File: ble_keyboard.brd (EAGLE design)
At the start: 50.7 x 23.2 mm, 23 parts, among them Q1 DMG6968U-7, Q2 DMG2305UX-7, U1 YJ-14015

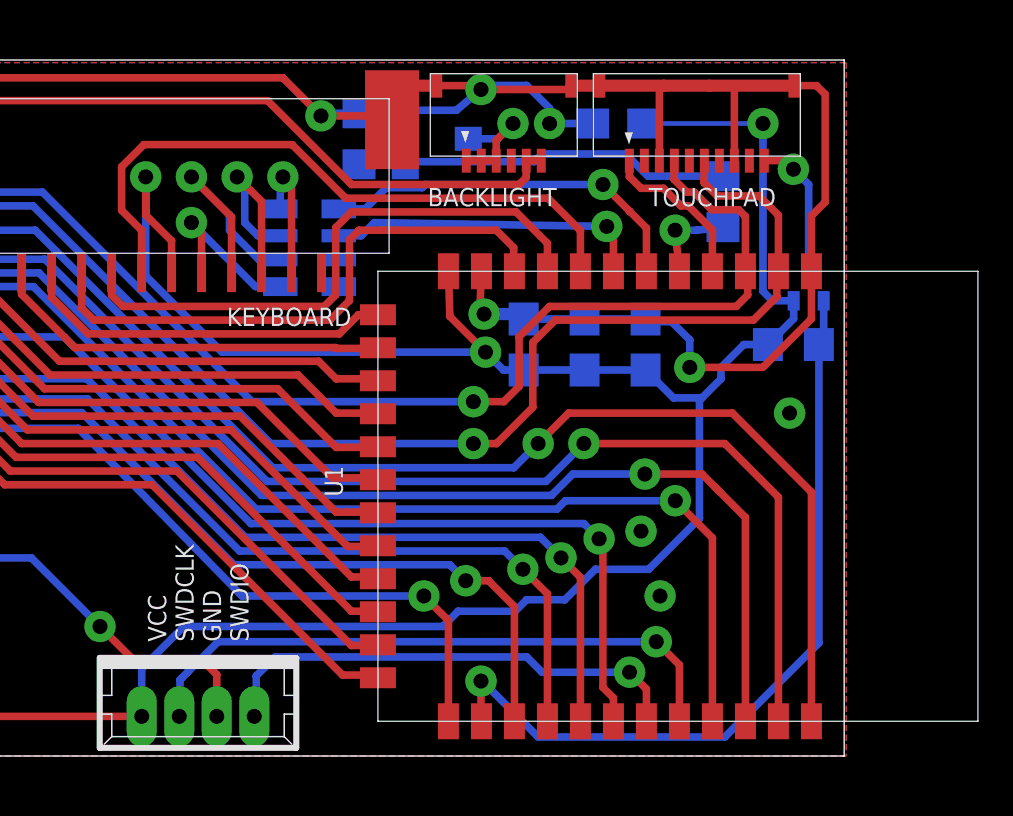
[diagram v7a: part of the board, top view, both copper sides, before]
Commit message: - Fix P ch FET footprint - Add a note about unconnected LEDs
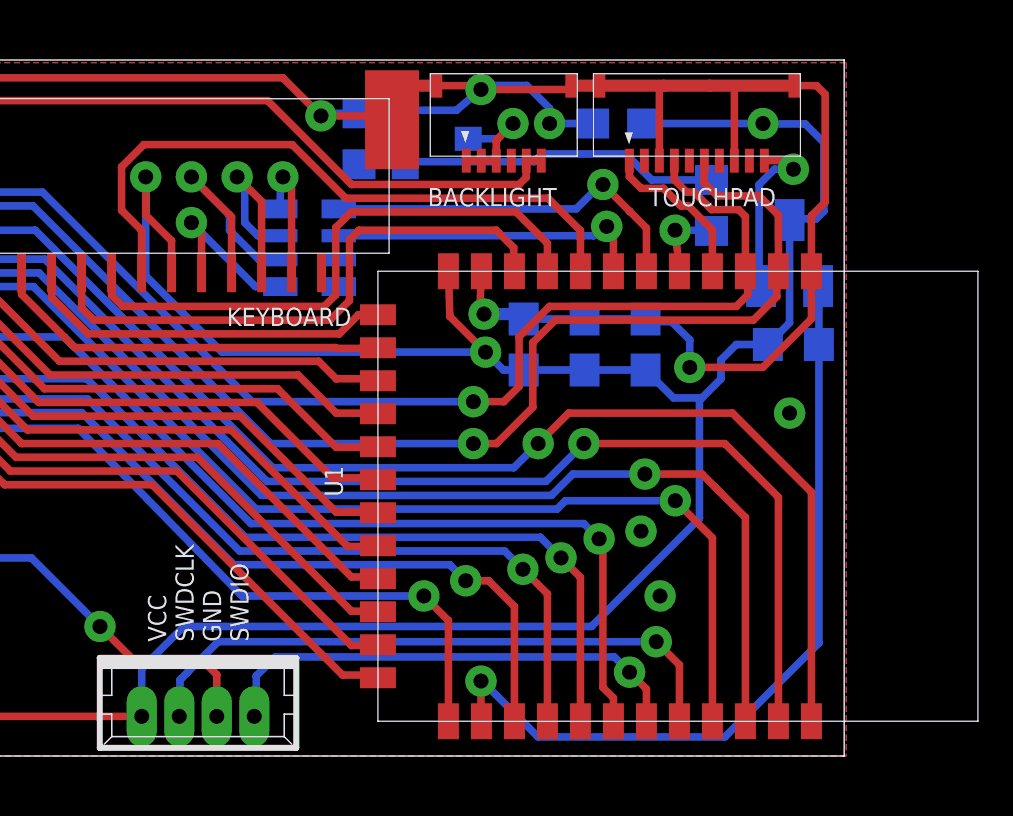
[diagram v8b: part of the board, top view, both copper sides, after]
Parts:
- Q2: device transistor-fet:SC75_INFINEON -> transistor-fet:SOT23
- moved Q2 1.20 mm to (48.9, 16.8)
- moved R2 0.40 mm to (46.3, 18.4)
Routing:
- net +3V3: track 96.9 -> 98.8 mm
- net V_TOUCHPAD: track 4.53 -> 5.85 mm
